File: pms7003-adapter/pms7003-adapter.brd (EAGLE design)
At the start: 36.7 x 20 mm, 4 parts, among them J1 LPPB052CFFN-RC

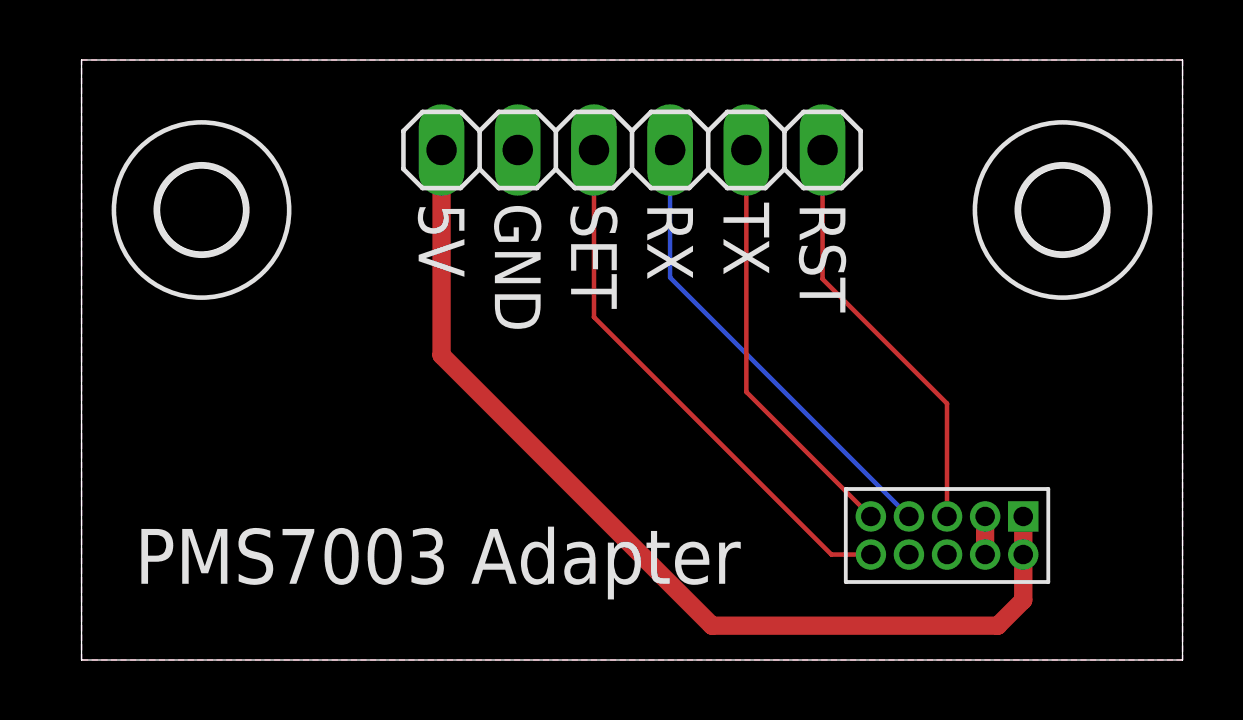
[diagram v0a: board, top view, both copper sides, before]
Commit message: Reduced size of the PMS7003 adapter, replaced THT header with SMD header
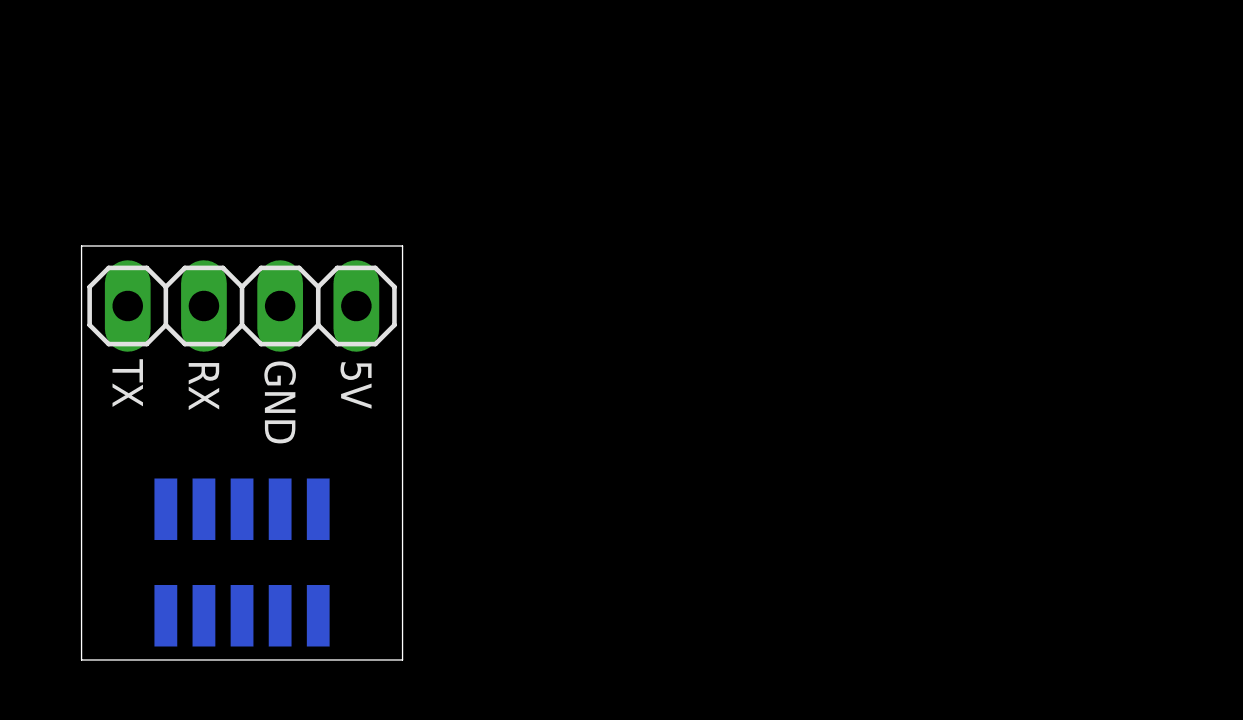
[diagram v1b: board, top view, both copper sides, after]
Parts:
- removed H1, H2: MOUNT-HOLE2.8, holes:2,8
- J1: value LPPB052CFFN-RC -> 20021321-00010C4LF; device aqm-parts:SULLINS_LPPB052CFFN-RC -> aqm-parts:AMPHENOL_20021321-00010C4LF
- J2: device pinhead:1X06 -> pinhead:1X04
- moved J1 23.5 mm to (5.35, 3.25), flipped to the bottom, turned to 90 degrees
- moved J2 14.0 mm to (5.35, 11.8), turned to 180 degrees
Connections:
- removed net RST: J1.5, J2.6
- removed net SET: J1.10, J2.3
- net RX: now also J1.8, J2.3; no longer J1.7, J2.4
- net TX: now also J1.10, J2.4; no longer J1.9, J2.5
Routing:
- net 5V: track 33.1 -> 0.00 mm
- net SET: track 18.1 -> 0.00 mm
- net RX: track 15.5 -> 0.00 mm
- net RST: track 13.9 -> 0.00 mm
- net TX: track 13.9 -> 0.00 mm
- net GND: track 1.27 -> 0.00 mm
- removed copper zone on layer 1, net GND
- removed copper zone on layer 16, net GND
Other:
- board size 36.7 x 20 mm -> 10.7 x 13.8 mm
- board text removed: "PMS7003 Adapter"
- board text removed: "RST"
- board text removed: "SET"
